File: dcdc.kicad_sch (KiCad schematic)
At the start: 199 parts, among them U11 SIC431AED-T1-GE3, U12 SIC431AED-T1-GE3, U13 SIC431AED-T1-GE3, U22 INA219AIDCNR, U50 INA219AIDCNR, U60 INA219AIDCNR, U65 SIC431AED-T1-GE3, U66 INA219AIDCNR, U69 TPS564247DRLR, U7 TPS564247DRLR, U75 SIC431AED-T1-GE3, U76 INA219AIDCNR, U8 SIC431AED-T1-GE3

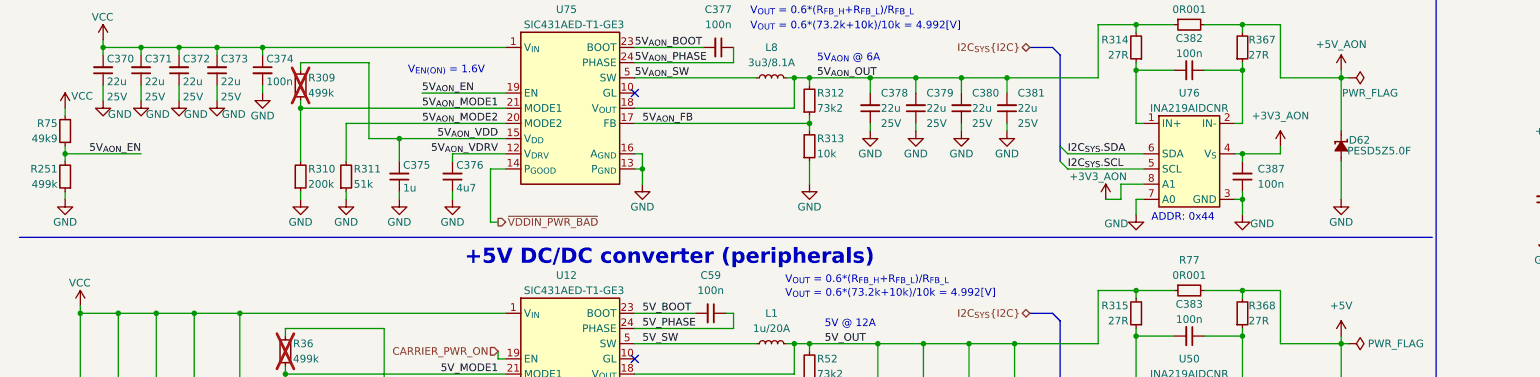
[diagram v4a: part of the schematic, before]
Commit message: [#88671] Fix 5VAON_EN resistor divider
Changed R251 value from 499k to 2k2 that results DC/DC converter (U75)
starts when Vcc >= 23.48V.
Added C6 capasitor as described in User's manual (100n 50V)
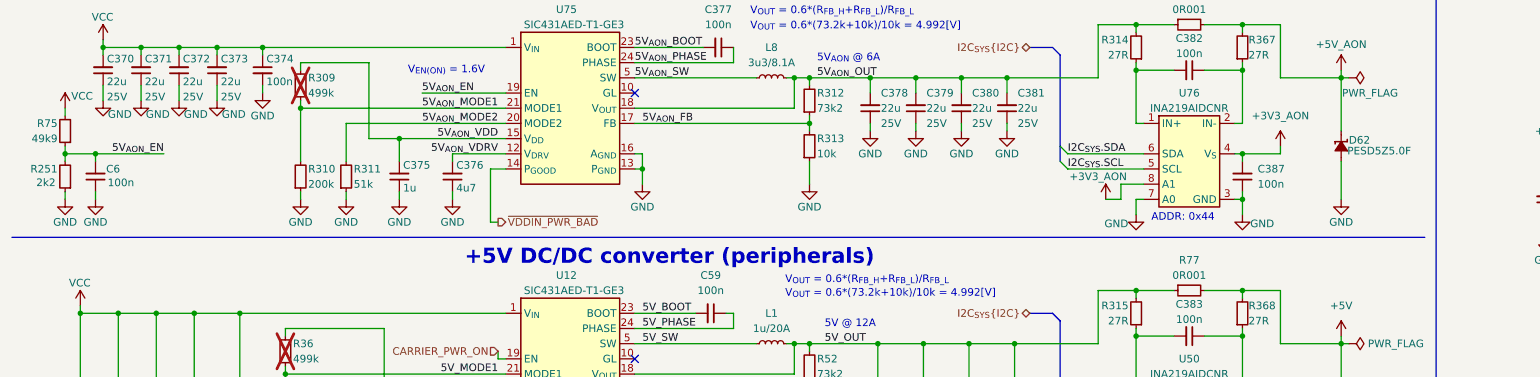
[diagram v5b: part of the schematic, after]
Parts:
- added C6: C_100n_0402, antmicro-footprints:C_0402_1005Metric, symbol antmicroCapacitors0402:C_100n_0402
- R251: symbol antmicroResistors0402:R_499k_0402 -> antmicroResistors0402:R_2k2_0402; MPN CR0402-FX-4993GLF -> CR0402-FX-2201GLF; Val 499k -> 2k2
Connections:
- net 5V_{AON}_EN: now also C6.2
- net GND: now also C6.1

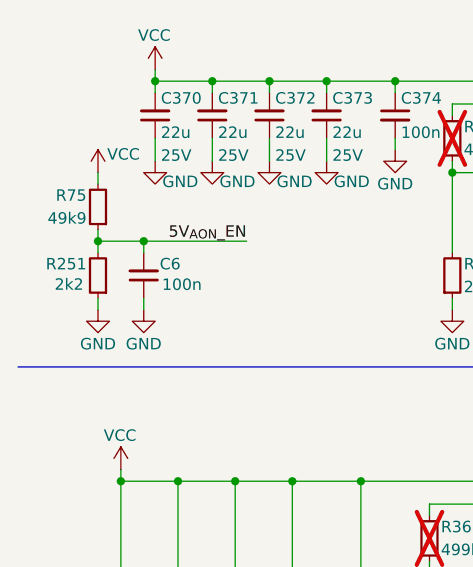
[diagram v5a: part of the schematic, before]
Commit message: [#88671] Fix 5VAON_EN resistor divider after review
Changed R251 value from 2k2 to 2k37 that results DC/DC converter (U75)
starts when Vcc >= 22.05V in best scenario, 22.48V in worst case
scenario.
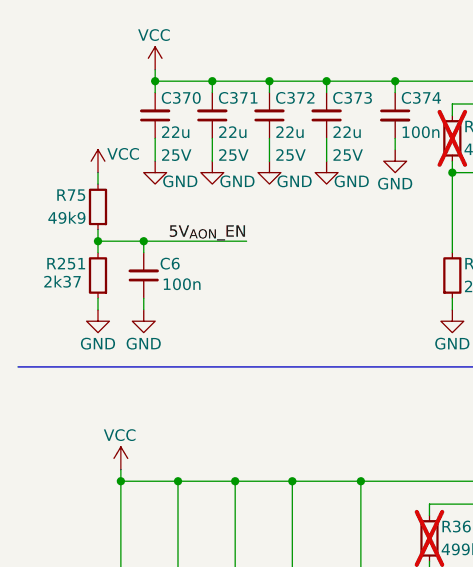
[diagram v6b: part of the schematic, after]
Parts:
- R251: symbol antmicroResistors0402:R_2k2_0402 -> antmicroResistors0402:R_2k37_0402; MPN CR0402-FX-2201GLF -> CR0402-FX-2371GLF; Val 2k2 -> 2k37
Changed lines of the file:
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@@
 	)
 	(symbol
-		(lib_id "antmicroResistors0402:R_2k2_0402")
+		(lib_id "antmicroResistors0402:R_2k37_0402")
 		(at 19.05 186.69 270)
 		(mirror x)
@@
 			)
 		)
-		(property "Description" "SMD Chip Resistor, 2.2 kohm, ± 1%, 62.5 mW, 0402 [1005 Metric], Thick Film, General Purpose"
+		(property "Description" "SMD Chip Resistor"
 			(at -11.43 166.37 0)
 			(effects
@@
 			)
 		)
-		(property "MPN" "CR0402-FX-2201GLF"
+		(property "MPN" "CR0402-FX-2371GLF"
 			(at -1.27 166.37 0)
 			(effects
@@
 			)
 		)
-		(property "Val" "2k2"
-			(at 14.224 184.404 90)
+		(property "Val" "2k37"
+			(at 12.954 184.15 90)
 			(effects
 				(font

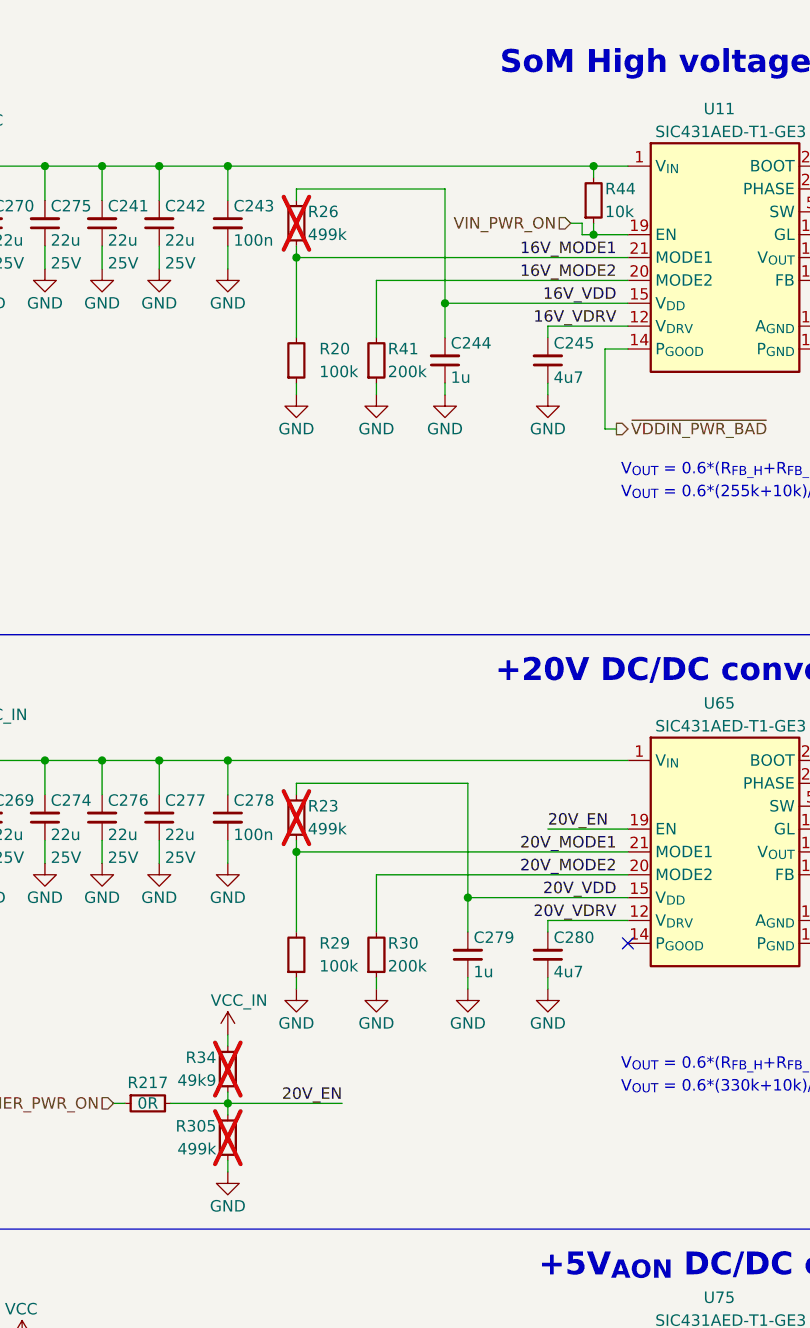
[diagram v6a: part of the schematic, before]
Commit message: [#88668] VIN_PWR_ON line fix
Removed Removed R45, Removed R44,Removed Q30
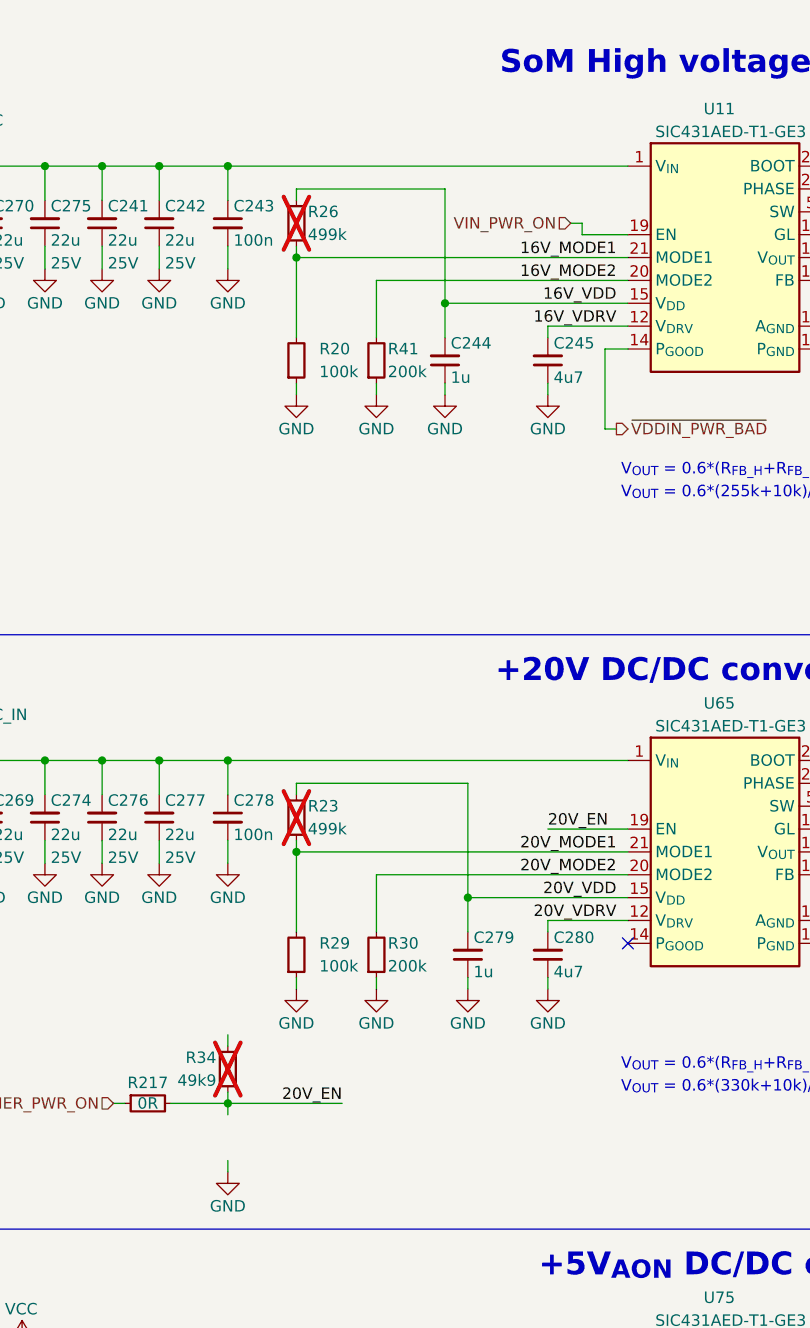
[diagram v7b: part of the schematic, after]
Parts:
- removed R305: R_499k_0402, antmicro-footprints:R_0402_1005Metric, symbol antmicroResistors0402:R_499k_0402
- removed R44: R_10k_0402, antmicro-footprints:R_0402_1005Metric, symbol antmicroResistors0402:R_10k_0402
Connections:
- net VCC_IN: no longer R34.2

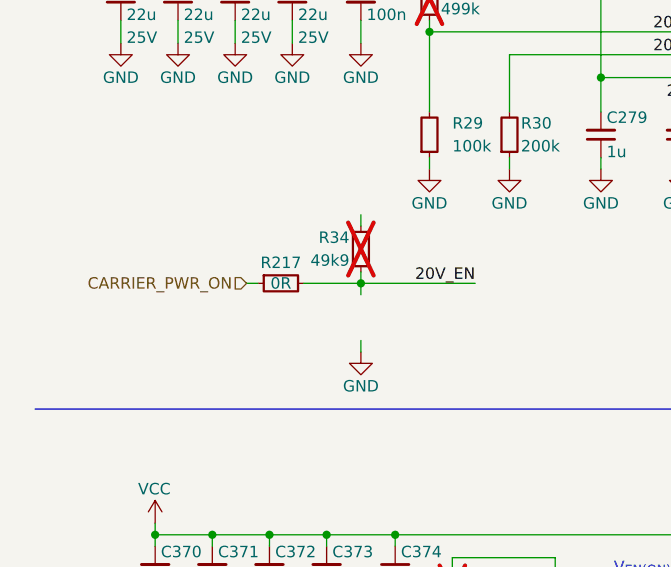
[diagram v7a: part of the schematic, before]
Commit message: [#88668] CARRIER_PWR_ON pull-up fix
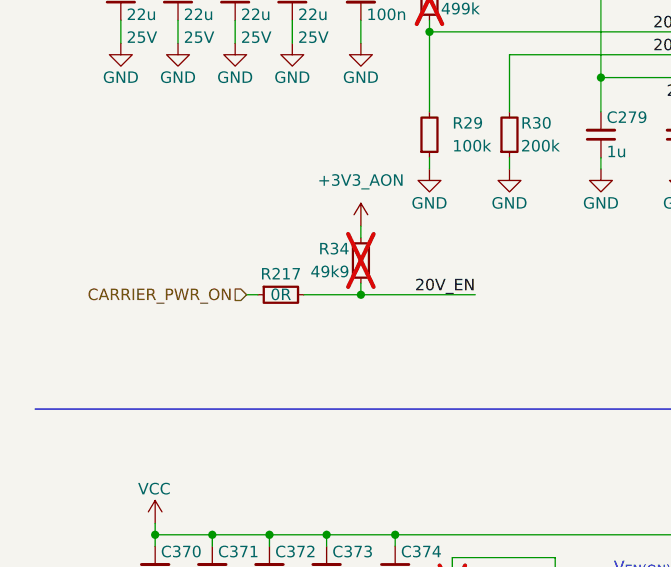
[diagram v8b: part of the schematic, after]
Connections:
- net +3V3_AON: now also R34.2
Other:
- moved on the sheet: R217, R34
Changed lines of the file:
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@@
 	)
 	(junction
-		(at 48.26 134.62)
+		(at 48.26 135.89)
 		(diameter 0)
 		(color 0 0 0 0)
@@
 	(wire
 		(pts
-			(xy 41.91 134.62) (xy 48.26 134.62)
+			(xy 41.91 135.89) (xy 48.26 135.89)
 		)
 		(stroke
@@
 	(wire
 		(pts
-			(xy 48.26 127) (xy 48.26 128.27)
+			(xy 48.26 128.27) (xy 48.26 129.54)
 		)
 		(stroke
@@
 	(wire
 		(pts
-			(xy 48.26 134.62) (xy 48.26 135.89)
-		)
-		(stroke
-			(width 0)
-			(type default)
-		)
-	)
-	(wire
-		(pts
 			(xy 64.77 219.71) (xy 92.71 219.71)
 		)
@@
 	(wire
 		(pts
-			(xy 35.56 134.62) (xy 36.83 134.62)
+			(xy 35.56 135.89) (xy 36.83 135.89)
 		)
 		(stroke
@@
 	(wire
 		(pts
-			(xy 48.26 134.62) (xy 60.96 134.62)
+			(xy 48.26 135.89) (xy 60.96 135.89)
 		)
 		(stroke
@@
 	(wire
 		(pts
-			(xy 48.26 133.35) (xy 48.26 134.62)
+			(xy 48.26 134.62) (xy 48.26 135.89)
 		)
 		(stroke
@@
 	(wire
 		(pts
-			(xy 48.26 140.97) (xy 48.26 142.24)
-		)
-		(stroke
-			(width 0)
-			(type default)
-		)
-	)
-	(wire
-		(pts
 			(xy 115.57 279.4) (xy 115.57 274.32)
 		)
@@
 	)
 	(label "20V_EN"
-		(at 60.96 134.62 180)
+		(at 60.96 135.89 180)
 		(effects
 			(font
@@
 	(hierarchical_label "CARRIER_PWR_ON"
 		(shape input)
-		(at 35.56 134.62 180)
+		(at 35.56 135.89 180)
 		(effects
 			(font
@@
 	(symbol
 		(lib_id "antmicroResistors0402:R_49k9_0402")
-		(at 48.26 133.35 270)
+		(at 48.26 134.62 270)
 		(mirror x)
 		(unit 1)
@@
 		(dnp yes)
 		(property "Reference" "R34"
-			(at 46.99 129.54 90)
+			(at 46.99 130.81 90)
 			(effects
 				(font
@@
 		)
 		(property "Value" "R_49k9_0402"
-			(at 35.56 113.03 0)
+			(at 35.56 114.3 0)
 			(effects
 				(font
@@
 		)
 		(property "Footprint" "antmicro-footprints:R_0402_1005Metric"
-			(at 33.02 113.03 0)
+			(at 33.02 114.3 0)
 			(effects
 				(font
@@
 		)
 		(property "Datasheet" "https://www.bourns.com/docs/product-datasheets/cr.pdf"
-			(at 30.48 113.03 0)
+			(at 30.48 114.3 0)
 			(effects
 				(font
@@
 		)
 		(property "Description" "SMD Chip Resistor, 49.9 kohm, ± 1%, 63 mW, 0402 [1005 Metric], Thick Film, General Purpose"
-			(at 48.26 133.35 0)
+			(at 48.26 134.62 0)
 			(effects
 				(font
@@
 		)
 		(property "MPN" "CR0402-FX-4992GLF"
-			(at 27.94 113.03 0)
+			(at 27.94 114.3 0)
 			(effects
 				(font
@@
 		)
 		(property "Manufacturer" "Bourns"
-			(at 25.4 113.03 0)
+			(at 25.4 114.3 0)
 			(effects
 				(font
@@
 		)
 		(property "License" "Apache-2.0"
-			(at 22.86 113.03 0)
+			(at 22.86 114.3 0)
 			(effects
 				(font
@@
 		)
 		(property "Author" "Antmicro"
-			(at 20.32 113.03 0)
+			(at 20.32 114.3 0)
 			(effects
 				(font
@@
 		)
 		(property "Val" "49k9"
-			(at 46.99 132.08 90)
+			(at 46.99 133.35 90)
 			(effects
 				(font
@@
 		)
 		(property "Tolerance" "1%"
-			(at 38.1 113.03 0)
+			(at 38.1 114.3 0)
 			(effects
 				(font
@@
 	)
 	(symbol
+		(lib_id "antmicropower:+3V3_AON")
+		(at 48.26 128.27 0)
+		(unit 1)
+		(exclude_from_sim no)
+		(in_bom yes)
+		(on_board yes)
+		(dnp no)
+		(property "Reference" "#PWR0147"
+			(at 48.26 132.08 0)
+			(effects
+				(font
+					(size 1.27 1.27)
+				)
+				(hide yes)
+			)
+		)
+		(property "Value" "+3V3_AON"
+			(at 48.26 123.19 0)
+			(effects
+				(font
+					(size 1.27 1.27)
+				)
+			)
+		)
+		(property "Footprint" ""
+			(at 48.26 128.27 0)
+			(effects
+				(font
+					(size 1.27 1.27)
+				)
+				(hide yes)
+			)
+		)
+		(property "Datasheet" ""
+			(at 48.26 128.27 0)
+			(effects
+				(font
+					(size 1.27 1.27)
+				)
+				(hide yes)
+			)
+		)
+		(property "Description" ""
+			(at 48.26 128.27 0)
+			(effects
+				(font
+					(size 1.27 1.27)
+				)
+				(hide yes)
+			)
+		)
+		(pin "1"
+		)
+		(instances
+			(project "jetson-agx-thor-baseboard"
+				(path "/f569b0be-0afd-48b7-93ee-28582a4c645c/24bfa3d1-0a03-41a0-8beb-0ef00bfb4ba3"
+					(reference "#PWR0147")
+					(unit 1)
+				)
+			)
+		)
+	)
+	(symbol
 		(lib_id "antmicropower:GND")
 		(at 170.18 279.4 0)
@@
 	)
 	(symbol
-		(lib_id "antmicropower:GND")
-		(at 48.26 142.24 0)
-		(unit 1)
-		(exclude_from_sim no)
-		(in_bom yes)
-		(on_board yes)
-		(dnp no)
-		(property "Reference" "#PWR0662"
-			(at 48.26 148.59 0)
-			(effects
-				(font
-					(size 1.27 1.27)
-				)
-				(justify left bottom)
-				(hide yes)
-			)
-		)
-		(property "Value" "GND"
-			(at 48.26 146.05 0)
-			(effects
-				(font
-					(size 1.27 1.27)
-					(thickness 0.15)
-				)
-			)
-		)
-		(property "Footprint" ""
-			(at 57.15 149.86 0)
-			(effects
-				(font
-					(size 1.27 1.27)
-					(thickness 0.15)
-				)
-				(justify left bottom)
-				(hide yes)
-			)
-		)
-		(property "Datasheet" ""
-			(at 57.15 154.94 0)
-			(effects
-				(font
-					(size 1.27 1.27)
-					(thickness 0.15)
-				)
-				(justify left bottom)
-				(hide yes)
-			)
-		)
-		(property "Description" ""
-			(at 48.26 142.24 0)
-			(effects
-				(font
-					(size 1.27 1.27)
-				)
-				(hide yes)
-			)
-		)
-		(property "Author" "Antmicro"
-			(at 57.15 149.86 0)
-			(effects
-				(font
-					(size 1.27 1.27)
-					(thickness 0.15)
-				)
-				(justify left bottom)
-				(hide yes)
-			)
-		)
-		(property "License" "Apache-2.0"
-			(at 57.15 152.4 0)
-			(effects
-				(font
-					(size 1.27 1.27)
-					(thickness 0.15)
-				)
-				(justify left bottom)
-				(hide yes)
-			)
-		)
-		(pin "1"
-		)
-		(instances
-			(project "jetson-agx-thor-baseboard"
-				(path "/f569b0be-0afd-48b7-93ee-28582a4c645c/24bfa3d1-0a03-41a0-8beb-0ef00bfb4ba3"
-					(reference "#PWR0662")
-					(unit 1)
-				)
-			)
-		)
-	)
-	(symbol
 		(lib_id "antmicroCapacitorsmisc:C_22u_25V_0805")
 		(at 177.8 73.66 90)
@@
 	(symbol
 		(lib_id "antmicroResistors0402:R_0R_0402")
-		(at 36.83 134.62 0)
+		(at 36.83 135.89 0)
 		(unit 1)
 		(exclude_from_sim no)
@@
 		(dnp no)
 		(property "Reference" "R217"
-			(at 39.37 132.334 0)
+			(at 39.37 133.604 0)
 			(effects
 				(font
@@
 		)
 		(property "Value" "R_0R_0402"
-			(at 57.15 147.32 0)
+			(at 57.15 148.59 0)
 			(effects
 				(font
@@
 		)
 		(property "Footprint" "antmicro-footprints:R_0402_1005Metric"
-			(at 57.15 149.86 0)
+			(at 57.15 151.13 0)
 			(effects
 				(font
@@
 		)
 		(property "Datasheet" "https://industrial.panasonic.com/cdbs/www-data/pdf/RDA0000/AOA0000C301.pdf"
-			(at 57.15 152.4 0)
+			(at 57.15 153.67 0)
 			(effects
 				(font
@@
 		)
 		(property "Description" "SMD Chip Resistor, Jumper, 0 ohm, 100 mW, 0402 [1005 Metric], Thick Film, General Purpose"
-			(at 57.15 167.64 0)
+			(at 57.15 168.91 0)
 			(effects
 				(font
@@
 		)
 		(property "MPN" "ERJ2GE0R00X"
-			(at 57.15 154.94 0)
+			(at 57.15 156.21 0)
 			(effects
 				(font
@@
 		)
 		(property "Manufacturer" "Panasonic"
-			(at 57.15 157.48 0)
+			(at 57.15 158.75 0)
 			(effects
 				(font
@@
 		)
 		(property "License" "Apache-2.0"
-			(at 57.15 160.02 0)
+			(at 57.15 161.29 0)
 			(effects
 				(font
@@
 		)
 		(property "Author" "Antmicro"
-			(at 57.15 162.56 0)
+			(at 57.15 163.83 0)
 			(effects
 				(font
@@
 		)
 		(property "Val" "0R"
-			(at 39.37 134.62 0)
+			(at 39.37 135.89 0)
 			(effects
 				(font
@@
 		)
 		(property "Tolerance" "~"
-			(at 57.15 144.78 0)
+			(at 57.15 146.05 0)
 			(effects
 				(font
@@
 		)
 		(property "Current" "1A"
-			(at 57.15 165.1 0)
+			(at 57.15 166.37 0)
 			(effects
 				(font
